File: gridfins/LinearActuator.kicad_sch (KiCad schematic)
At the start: 0 parts

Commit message: SD card, linear actuator encoders
Imported microSD reader from Stark

Added pin connectors and SPI routes for AS5048 magnetic rotary encoder to be used with the linear actuator/brushed motor

Added test pads for SD reader and encoder chip select
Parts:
- added J7: Conn_01x06_Pin, symbol Connector:Conn_01x06_Pin
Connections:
- new net +3.3V: J7.5 (Pin_5)
- new net ENCODER_CS: J7.4 (Pin_4)
- new net GND: J7.6 (Pin_6)
- new net VSPI_MISO: J7.1 (Pin_1)
- new net VSPI_MOSI: J7.2 (Pin_2)
- new net VSPI_SCLK: J7.3 (Pin_3)
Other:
- note added: "Connectors for AS5048 magnetic Rotary Encoder - for linear actuator brushed motor"

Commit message: deleted obsolete ICM-20608-G from IMU, added WSEN-ISDS adviced by Jack, a 6 axis IMU. Added footprint and symbol. Yet to finish connections and finish the "application circuit". Added footprint for 6pin connector in Linear Actuator sheet.
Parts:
- J7: footprint (none) -> Connector_PinHeader_2.54mm:PinHeader_1x06_P2.54mm_Vertical
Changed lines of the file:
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@@
 			)
 		)
-		(property "Footprint" ""
+		(property "Footprint" "Connector_PinHeader_2.54mm:PinHeader_1x06_P2.54mm_Vertical"
 			(at 85.09 72.39 0)
 			(effects

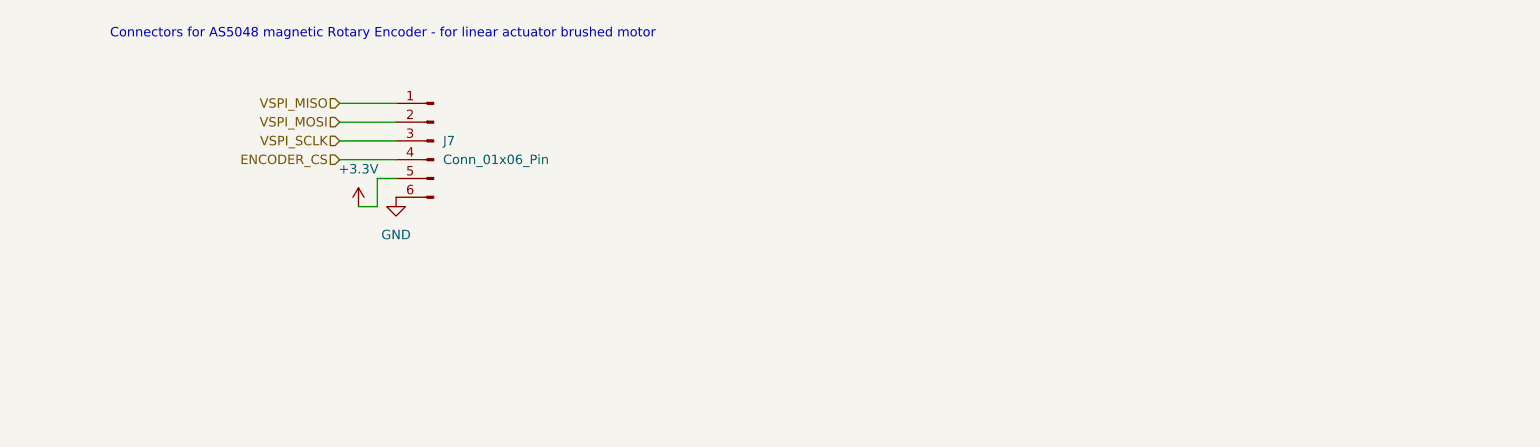
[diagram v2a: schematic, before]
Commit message: First Attempt connection of stepper motor driver for linear actuator
Added connections of driver and 4 pin nano. Added hierarchical labels and connected to GPIO. Current configuration is the INDEX mode
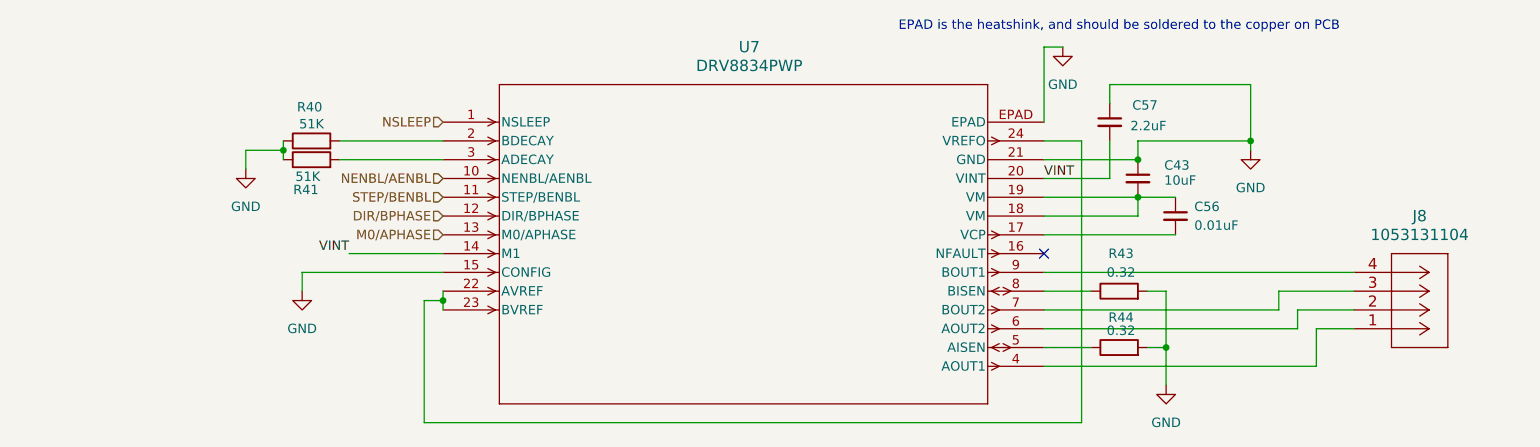
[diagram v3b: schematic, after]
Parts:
- removed J7: Conn_01x06_Pin, Connector_PinHeader_2.54mm:PinHeader_1x06_P2.54mm_Vertical, symbol Connector:Conn_01x06_Pin
- added C43: 10uF, symbol Device:C_Small
- added C56: 0.01uF, symbol Device:C_Small
- added C57: 2.2uF, symbol Device:C_Small
- added J8: 1053131104, CON_1053131104, symbol iclr:1053131104
- added R40, R41: 51K, symbol Device:R
- added R43, R44: 0.32, symbol Device:R
- added U7: DRV8834PWP, PWP_24, symbol iclr:DRV8834PWP
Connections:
- net GND: now also C43.1, C57.1, R40.1, R41.1, R43.2, R44.2, U7.15 (CONFIG), U7.21 (GND), U7.EPAD
- new net: J8.1, U7.4 (AOUT1)
- new net: J8.2, U7.6 (AOUT2)
- new net: J8.3, U7.7 (BOUT2)
- new net: J8.4, U7.9 (BOUT1)
- new net: R43.1, U7.8 (BISEN)
- new net: R40.2, U7.2 (BDECAY)
- new net: C56.2, U7.17 (VCP)
- new net: C43.2, C56.1, U7.18 (VM), U7.19 (VM)
- new net: U7.22 (AVREF), U7.23 (BVREF), U7.24 (VREFO)
- new net: R41.2, U7.3 (ADECAY)
- new net: R44.1, U7.5 (AISEN)
- new net DIR/BPHASE: U7.12 (DIR/BPHASE)
- new net M0/APHASE: U7.13 (M0/APHASE)
- new net NENBL/AENBL: U7.10 (NENBL/AENBL)
- new net NSLEEP: U7.1 (NSLEEP)
- new net STEP/BENBL: U7.11 (STEP/BENBL)
- new net VINT: C57.2, U7.14 (M1), U7.20 (VINT)
- no-connect marks 0 -> 1
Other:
- note added: "EPAD is the heatshink, and should be soldered to the copper on PCB"
- note removed: "Connectors for AS5048 magnetic Rotary Encoder - for linear actuator brushed motor"

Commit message: Power distribution rework
Added missing main power supply voltage to Stepper Motor Driver Board

Separate Buck converter for servo and linear actuator(stepper motor)

16.8V -> Buck -> high side switch -> H-bridge -> 10V
16.8V -> Buck -> Servo -> 7.4V
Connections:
- net VM: now reaches C43.2, C56.1, U7.18 (VM), U7.19 (VM)
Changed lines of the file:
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@@
+	)
+	(junction
+		(at 185.42 80.01)
+		(diameter 0)
+		(color 0 0 0 0)
 	)
 	(junction
@@
 		(pts
 			(xy 184.15 100.33) (xy 181.61 100.33)
+		)
+		(stroke
+			(width 0)
+			(type default)
+		)
+	)
+	(wire
+		(pts
+			(xy 185.42 80.01) (xy 201.93 80.01)
 		)
 		(stroke
@@
 		)
 	)
+	(hierarchical_label "VM"
+		(shape input)
+		(at 201.93 80.01 0)
+		(effects
+			(font
+				(size 1.27 1.27)
+			)
+			(justify left)
+		)
+	)

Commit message: PCB + schematic updates
Solved footprint error which prevented PCB from updating

Deleted old buck converter PCB design (old buck now replaced with 2 for servo and linear acc)

Moved Snubber and crossed out capacitor network to the backside of board

Unsure whether if the +10V routing is valid - currently connected via tracers, not planes (may be a problem for current)

Restructured old pcb which previously had planes associated with no nets (assigned nets to them)

If current design approved, will proceed to carry out the same design for the servo controlling buck converter.
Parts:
- C43, C56, C57: footprint (none) -> Capacitor_SMD:C_0402_1005Metric
- J8: footprint CON_1053131104 -> Connector_Molex:Molex_Nano-Fit_105309-xx04_1x04_P2.50mm_Vertical
- R40, R41, R43, R44: footprint (none) -> Resistor_SMD:R_0402_1005Metric
- U7: footprint PWP_24 -> iclr:PWP_24
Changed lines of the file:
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@@
 			)
 		)
-		(property "Footprint" "CON_1053131104"
+		(property "Footprint" "Connector_Molex:Molex_Nano-Fit_105309-xx04_1x04_P2.50mm_Vertical"
 			(at 219.71 91.186 0)
 			(effects
@@
 			)
 		)
-		(property "Footprint" ""
+		(property "Footprint" "Resistor_SMD:R_0402_1005Metric"
 			(at 177.8 94.488 90)
 			(effects
@@
 			)
 		)
-		(property "Footprint" ""
+		(property "Footprint" "Resistor_SMD:R_0402_1005Metric"
 			(at 68.58 74.168 90)
 			(effects
@@
 			)
 		)
-		(property "Footprint" "PWP_24"
+		(property "Footprint" "iclr:PWP_24"
 			(at 86.36 69.85 0)
 			(effects
@@
 			)
 		)
-		(property "Footprint" ""
+		(property "Footprint" "Capacitor_SMD:C_0402_1005Metric"
 			(at 180.34 77.47 0)
 			(effects
@@
 			)
 		)
-		(property "Footprint" ""
+		(property "Footprint" "Resistor_SMD:R_0402_1005Metric"
 			(at 68.58 76.708 90)
 			(effects
@@
 			)
 		)
-		(property "Footprint" ""
+		(property "Footprint" "Capacitor_SMD:C_0402_1005Metric"
 			(at 185.42 82.55 0)
 			(effects
@@
 			)
 		)
-		(property "Footprint" ""
+		(property "Footprint" "Capacitor_SMD:C_0402_1005Metric"
 			(at 176.53 69.85 0)
 			(effects
@@
 			)
 		)
-		(property "Footprint" ""
+		(property "Footprint" "Resistor_SMD:R_0402_1005Metric"
 			(at 177.8 102.108 90)
 			(effects

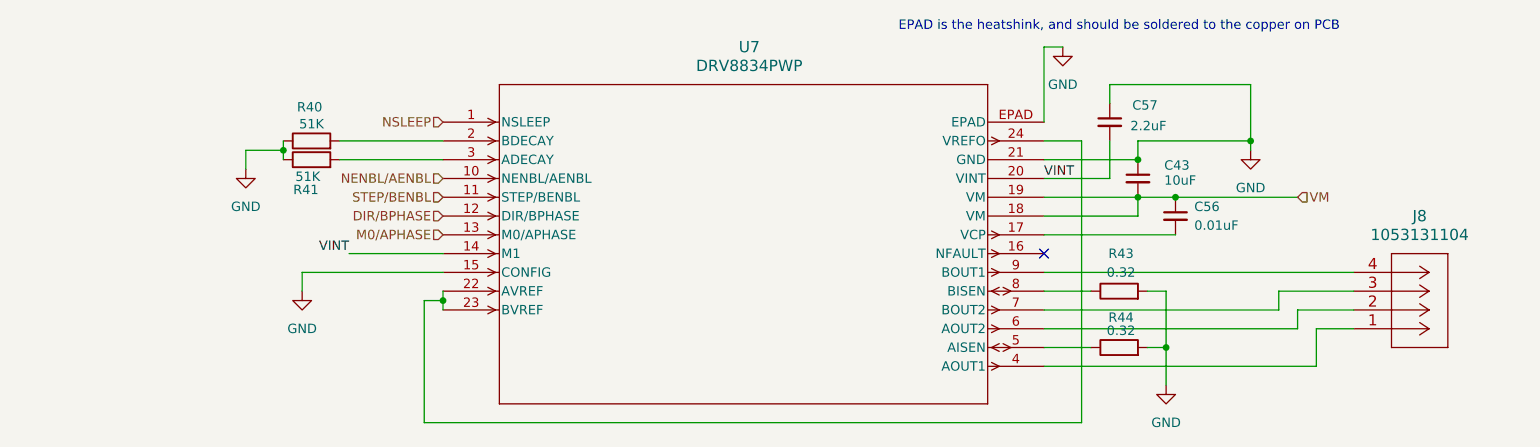
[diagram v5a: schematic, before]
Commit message: Handoff
implemented changes advised by Will. Still a bit unsure about how the EPAD should be connected to ground. The PCB design of both buck converters for servo and Hbridge(linear accuator) was completed - but still needs to be reviewed
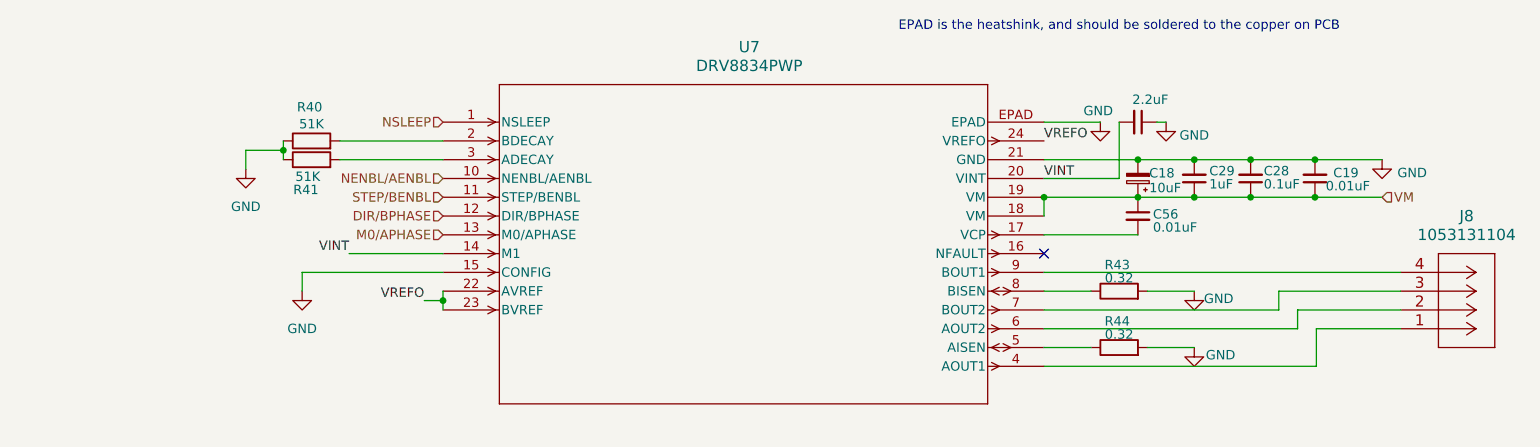
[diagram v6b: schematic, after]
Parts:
- removed C43: 10uF, Capacitor_SMD:C_0402_1005Metric, symbol Device:C_Small
- added C18: 10uF, Capacitor_SMD:C_0402_1005Metric, symbol Device:C_Polarized_Small
- added C19: 0.01uF, Capacitor_SMD:C_0402_1005Metric, symbol Device:C_Small
- added C28: 0.1uF, Capacitor_SMD:C_0402_1005Metric, symbol Device:C_Small
- added C29: 1uF, Capacitor_SMD:C_0402_1005Metric, symbol Device:C_Small
- J8: footprint Connector_Molex:Molex_Nano-Fit_105309-xx04_1x04_P2.50mm_Vertical -> Connector_Molex:Molex_Nano-Fit_105313-xx04_1x04_P2.50mm_Horizontal
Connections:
- net GND: now also C18.2, C19.2, C28.2, C29.2
- net VM: now also C18.1, C19.1, C28.1, C29.1
- net VREFO: now reaches U7.22 (AVREF), U7.23 (BVREF), U7.24 (VREFO)
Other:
- moved on the sheet: C56, J8
